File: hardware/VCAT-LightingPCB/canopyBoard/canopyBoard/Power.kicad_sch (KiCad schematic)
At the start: 8 parts

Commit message: added current check, please dont overwrite my file again
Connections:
- net PP/Vin: no longer names the net of F7.1, JP4.1 (A)
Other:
- removed sheet PP
- added sheet PowerProtection (PowerProtection.kicad_sch)
- moved on the sheet: JP4
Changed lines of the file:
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@@
 	)
 	(junction
-		(at 109.22 71.12)
+		(at 107.95 71.12)
 		(diameter 0)
 		(color 0 0 0 0)
@@
 	(wire
 		(pts
-			(xy 96.52 64.77) (xy 92.71 64.77)
+			(xy 95.25 64.77) (xy 92.71 64.77)
 		)
 		(stroke
@@
 	(wire
 		(pts
-			(xy 106.68 64.77) (xy 109.22 64.77)
+			(xy 105.41 64.77) (xy 107.95 64.77)
 		)
 		(stroke
@@
 	(wire
 		(pts
-			(xy 106.68 71.12) (xy 109.22 71.12)
+			(xy 106.68 71.12) (xy 116.84 71.12)
 		)
 		(stroke
@@
 	(wire
 		(pts
-			(xy 109.22 64.77) (xy 109.22 71.12)
+			(xy 107.95 64.77) (xy 107.95 71.12)
 		)
 		(stroke
@@
 		(pts
 			(xy 147.32 66.04) (xy 147.32 71.12)
-		)
-		(stroke
-			(width 0)
-			(type default)
-		)
-	)
-	(wire
-		(pts
-			(xy 109.22 71.12) (xy 116.84 71.12)
 		)
 		(stroke
@@
 	(symbol
 		(lib_id "Jumper:SolderJumper_2_Open")
-		(at 101.6 64.77 0)
+		(at 100.33 64.77 0)
 		(unit 1)
 		(body_style 1)
@@
 		(fields_autoplaced yes)
 		(property "Reference" "JP4"
-			(at 101.6 60.96 0)
+			(at 100.33 60.96 0)
 			(show_name no)
 			(do_not_autoplace no)
@@
 		)
 		(property "Value" "SolderJumper_2_Open"
-			(at 101.6 60.96 0)
+			(at 100.33 60.96 0)
 			(hide yes)
 			(show_name no)
@@
 		)
 		(property "Footprint" ""
-			(at 101.6 64.77 0)
+			(at 100.33 64.77 0)
 			(hide yes)
 			(show_name no)
@@
 		)
 		(property "Datasheet" ""
-			(at 101.6 72.39 0)
+			(at 100.33 72.39 0)
 			(hide yes)
 			(show_name no)
@@
 		)
 		(property "Description" "Solder Jumper, 2-pole, open"
-			(at 101.6 69.85 0)
+			(at 100.33 69.85 0)
 			(hide yes)
 			(show_name no)
@@
 	)
 	(sheet
+		(at 93.98 67.31)
+		(size 12.7 6.35)
+		(exclude_from_sim no)
+		(in_bom yes)
+		(on_board yes)
+		(dnp no)
+		(stroke
+			(width 0.1524)
+			(type solid)
+		)
+		(fill
+			(color 0 0 0 0)
+		)
+		(property "Sheetname" "PowerProtection"
+			(at 93.218 75.946 0)
+			(show_name no)
+			(do_not_autoplace no)
+			(effects
+				(font
+					(size 1.27 1.27)
+				)
+				(justify left bottom)
+			)
+		)
+		(property "Sheetfile" "PowerProtection.kicad_sch"
+			(at 93.98 74.2446 0)
+			(hide yes)
+			(show_name no)
+			(do_not_autoplace no)
+			(effects
+				(font
+					(size 1.27 1.27)
+				)
+				(justify left top)
+			)
+		)
+		(instances
+			(project "canopyBoard"
+				(path "/df5034a6-89e6-4596-8ae4-d16cb76dc299/9ffeb37d-6ae4-4995-919e-8c4714edda92"
+					(page "4")
+				)
+			)
+		)
+	)
+	(sheet
 		(at 116.84 68.58)
 		(size 25.4 12.7)
@@
 				)
 			)
-		)
-	)
-	(sheet
-		(at 93.98 68.58)
-		(size 12.7 12.7)
-		(exclude_from_sim no)
-		(in_bom yes)
-		(on_board yes)
-		(dnp no)
-		(stroke
-			(width 0.1524)
-			(type solid)
-		)
-		(fill
-			(color 0 0 0 0)
-		)
-		(property "Sheetname" "PP"
-			(at 93.98 67.8684 0)
-			(show_name no)
-			(do_not_autoplace no)
-			(effects
-				(font
-					(size 1.27 1.27)
-				)
-				(justify left bottom)
-			)
-		)
-		(property "Sheetfile" "PowerProtection.kicad_sch"
-			(at 78.232 84.836 0)
-			(hide yes)
-			(show_name no)
-			(do_not_autoplace no)
-			(effects
-				(font
-					(size 1.27 1.27)
-				)
-				(justify left top)
-			)
-		)
-		(pin "GND" input
-			(at 106.68 80.01 0)
-			(effects
-				(font
-					(size 1.27 1.27)
-				)
-				(justify right)
-			)
-		)
-		(pin "Vin" input
-			(at 93.98 71.12 180)
-			(effects
-				(font
-					(size 1.27 1.27)
-				)
-				(justify left)
-			)
-		)
-		(pin "Vout" output
-			(at 106.68 71.12 0)
-			(effects
-				(font
-					(size 1.27 1.27)
-				)
-				(justify right)
-			)
-		)
-		(instances
-			(project "canopyBoard"
-				(path "/df5034a6-89e6-4596-8ae4-d16cb76dc299/9ffeb37d-6ae4-4995-919e-8c4714edda92"
-					(page "4")
-				)
-			)

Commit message: please no overrides, complete with bus, hopefully
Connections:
- net PP/Vin: now reaches F7.1, JP4.1 (A)
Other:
- removed sheet 12VBuck1
- removed sheet PowerProtection
- added sheet 12VBuck (12VBuck.kicad_sch)
- added sheet PP (PP.kicad_sch)
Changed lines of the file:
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@@
+	(wire
+		(pts
+			(xy 142.24 78.74) (xy 143.51 78.74)
+		)
+		(stroke
+			(width 0)
+			(type default)
+		)
+	)
 	(wire
 		(pts
@@
 	(wire
 		(pts
-			(xy 106.68 80.01) (xy 107.95 80.01)
+			(xy 106.68 74.93) (xy 107.95 74.93)
 		)
 		(stroke
@@
 		(pts
 			(xy 83.82 71.12) (xy 85.09 71.12)
-		)
-		(stroke
-			(width 0)
-			(type default)
-		)
-	)
-	(wire
-		(pts
-			(xy 142.24 80.01) (xy 143.51 80.01)
 		)
 		(stroke
@@
 	(hierarchical_label "GND"
 		(shape bidirectional)
-		(at 143.51 80.01 0)
+		(at 143.51 78.74 0)
 		(effects
 			(font
@@
 	(hierarchical_label "GND"
 		(shape bidirectional)
-		(at 107.95 80.01 0)
+		(at 107.95 74.93 0)
 		(effects
 			(font
@@
 	)
 	(sheet
-		(at 93.98 67.31)
-		(size 12.7 6.35)
+		(at 116.84 68.58)
+		(size 25.4 11.43)
 		(exclude_from_sim no)
 		(in_bom yes)
@@
 			(color 0 0 0 0)
 		)
-		(property "Sheetname" "PowerProtection"
-			(at 93.218 75.946 0)
+		(property "Sheetname" "12VBuck"
+			(at 134.366 68.072 0)
 			(show_name no)
 			(do_not_autoplace no)
@@
 			)
 		)
-		(property "Sheetfile" "PowerProtection.kicad_sch"
-			(at 93.98 74.2446 0)
+		(property "Sheetfile" "12VBuck.kicad_sch"
+			(at 116.84 75.5146 0)
 			(hide yes)
 			(show_name no)
@@
 			)
 		)
-		(instances
-			(project "canopyBoard"
-				(path "/df5034a6-89e6-4596-8ae4-d16cb76dc299/9ffeb37d-6ae4-4995-919e-8c4714edda92"
-					(page "4")
-				)
-			)
-		)
-	)
-	(sheet
-		(at 116.84 68.58)
-		(size 25.4 12.7)
-		(exclude_from_sim no)
-		(in_bom yes)
-		(on_board yes)
-		(dnp no)
-		(stroke
-			(width 0.1524)
-			(type solid)
-		)
-		(fill
-			(color 0 0 0 0)
-		)
-		(property "Sheetname" "12VBuck1"
-			(at 133.858 67.818 0)
-			(show_name no)
-			(do_not_autoplace no)
-			(effects
-				(font
-					(size 1.27 1.27)
-				)
-				(justify left bottom)
-			)
-		)
-		(property "Sheetfile" "12VBuck.kicad_sch"
-			(at 116.84 81.8646 0)
-			(hide yes)
-			(show_name no)
-			(do_not_autoplace no)
-			(effects
-				(font
-					(size 1.27 1.27)
-				)
-				(justify left top)
-			)
-		)
 		(pin "GND" input
-			(at 142.24 80.01 0)
+			(at 142.24 78.74 0)
 			(effects
 				(font
@@
 				)
 			)
+		)
+	)
+	(sheet
+		(at 93.98 68.58)
+		(size 12.7 7.62)
+		(exclude_from_sim no)
+		(in_bom yes)
+		(on_board yes)
+		(dnp no)
+		(fields_autoplaced yes)
+		(stroke
+			(width 0.1524)
+			(type solid)
+		)
+		(fill
+			(color 0 0 0 0)
+		)
+		(property "Sheetname" "PP"
+			(at 93.98 67.8684 0)
+			(show_name no)
+			(do_not_autoplace no)
+			(effects
+				(font
+					(size 1.27 1.27)
+				)
+				(justify left bottom)
+			)
+		)
+		(property "Sheetfile" "PP.kicad_sch"
+			(at 93.98 76.7846 0)
+			(hide yes)
+			(show_name no)
+			(do_not_autoplace no)
+			(effects
+				(font
+					(size 1.27 1.27)
+				)
+				(justify left top)
+			)
+		)
+		(pin "GND" input
+			(at 106.68 74.93 0)
+			(effects
+				(font
+					(size 1.27 1.27)
+				)
+				(justify right)
+			)
+		)
+		(pin "Vin" input
+			(at 93.98 71.12 180)
+			(effects
+				(font
+					(size 1.27 1.27)
+				)
+				(justify left)
+			)
+		)
+		(pin "Vout" output
+			(at 106.68 71.12 0)
+			(effects
+				(font
+					(size 1.27 1.27)
+				)
+				(justify right)
+			)
+		)
+		(instances
+			(project "canopyBoard"
+				(path "/df5034a6-89e6-4596-8ae4-d16cb76dc299/9ffeb37d-6ae4-4995-919e-8c4714edda92"
+					(page "6")
+				)
+			)

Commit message: pray for no errors, more stuff to add
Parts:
- removed F7: Fuse, MyParts:3557-2, symbol Device:Fuse
- removed JP4: SolderJumper_2_Open, symbol Jumper:SolderJumper_2_Open
- removed R67: 16k, symbol Device:R
- removed R68: 4.7K, symbol Device:R
- removed TP26: TP_12V, symbol Connector:TestPoint
- removed TP27: TP_5V_VIN1, symbol Connector:TestPoint
- removed TP28: TP_5V_MUX, symbol Connector:TestPoint
- removed TP29: TP_3.3V, symbol Connector:TestPoint
- added F3: 1A, MyParts:3557-2, symbol Device:Fuse
- added JP1: SolderJumper_2_Open, Connector_PinHeader_2.54mm:PinHeader_1x02_P2.54mm_Vertical, symbol Jumper:SolderJumper_2_Open
- added R27: 16k, Resistor_SMD:R_0603_1608Metric_Pad0.98x0.95mm_HandSolder, symbol Device:R
- added R28: 4.7K, Resistor_SMD:R_0603_1608Metric_Pad0.98x0.95mm_HandSolder, symbol Device:R
- added TP10: TP_12V, LHRS_Special:TestPoint_HEX_3mmID, symbol lhrs_misc:Multimeter_TP
- added TP11: TP_5V_VIN1, LHRS_Special:TestPoint_HEX_3mmID, symbol lhrs_misc:Multimeter_TP
- added TP12: TP_5V_MUX, LHRS_Special:TestPoint_HEX_3mmID, symbol lhrs_misc:Multimeter_TP
- added TP13: TP_3.3V, LHRS_Special:TestPoint_HEX_3mmID, symbol lhrs_misc:Multimeter_TP
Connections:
- net 3.3V: now also TP13.1
- net 5V: now also TP12.1
- net GND: now also R28.2
- net PP/Vin: now also F3.1, JP1.1 (A)
- net V_IN: now also F3.2
- new net +12V_PP: JP1.2 (B), TP10.1
- new net 12VBuck/V_out_5V: R27.1, TP11.1
- new net Power_Mux/PR1: R27.2, R28.1
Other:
- removed sheet LDO2
- removed sheet Power_Mux1
- added sheet LDO (LDO.kicad_sch)
- added sheet Power_Mux (Power_Mux.kicad_sch)
- note added: "POWER"
- note removed: "Power Protection (UV/OV, OC, PTC)"
- note removed: "Power Regulation (12V -> 5V -> 3.3V)"

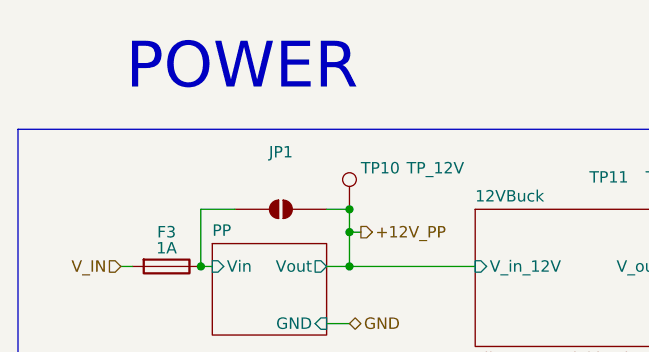
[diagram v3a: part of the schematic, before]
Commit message: Untrack KiCad .history, convert KiCAD-Sharepoint to a submodule, remove LightsPCB
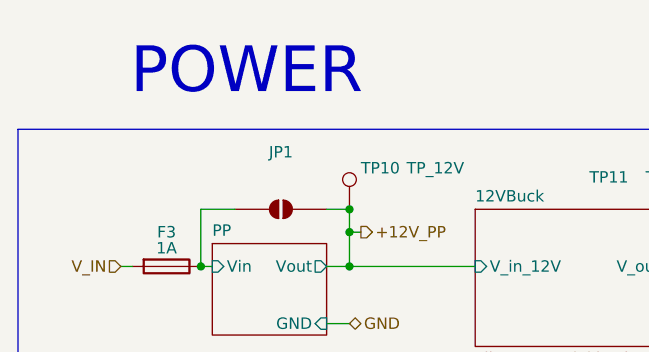
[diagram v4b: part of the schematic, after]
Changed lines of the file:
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@@
 	(text "POWER"
 		(exclude_from_sim no)
-		(at 59.182 41.402 0)
+		(at 59.69 41.91 0)
 		(effects
 			(font
